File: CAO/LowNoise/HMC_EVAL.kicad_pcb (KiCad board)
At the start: 2 copper layers, 71 x 83 mm, 57 parts, among them J1 Conn_01x03, J2 Conn_01x03, Q1 IRF7319IPBF, SW1 SW_Push, U1 OPA2209, U2 HMC1001, U4 INA128

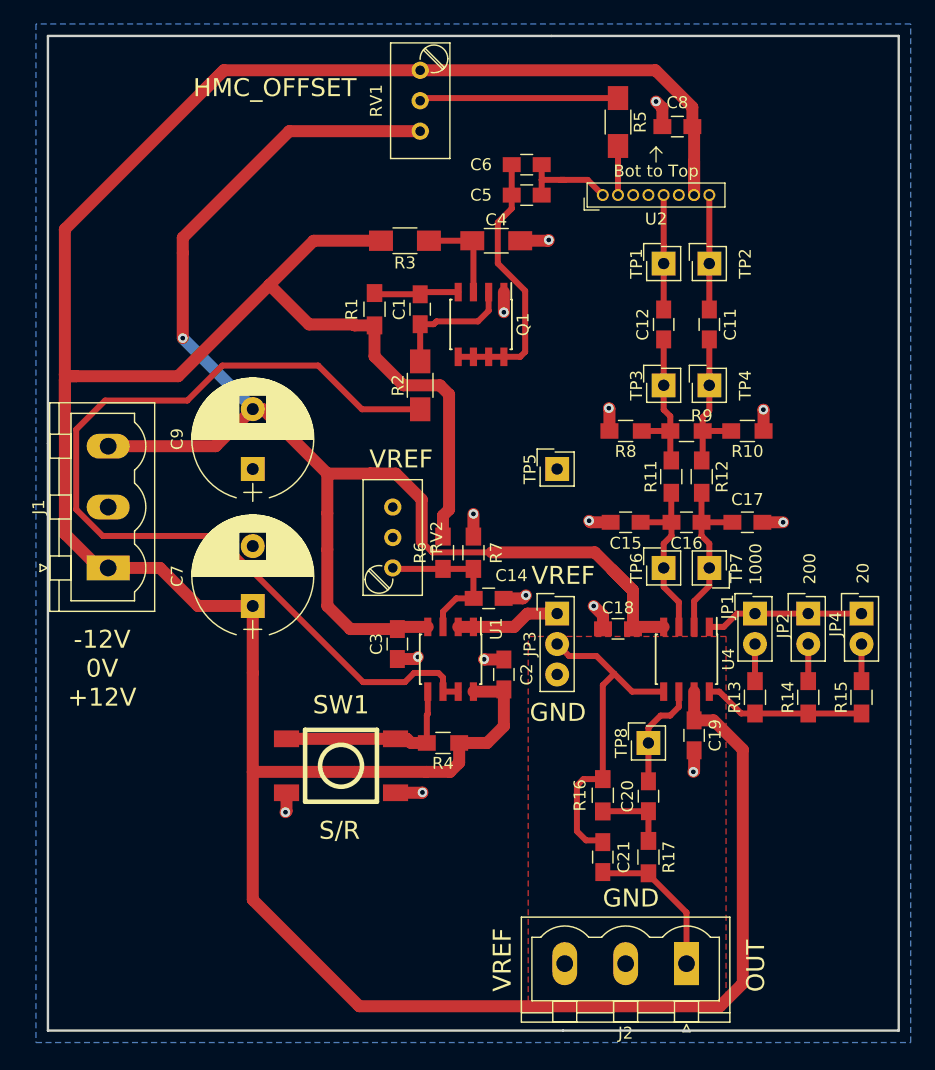
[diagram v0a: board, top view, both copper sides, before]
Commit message: - Low noise version is finish. - Add serigraphi on two design. - Qestion: Copper plane will block low freqency(200hz) magnetic wave??
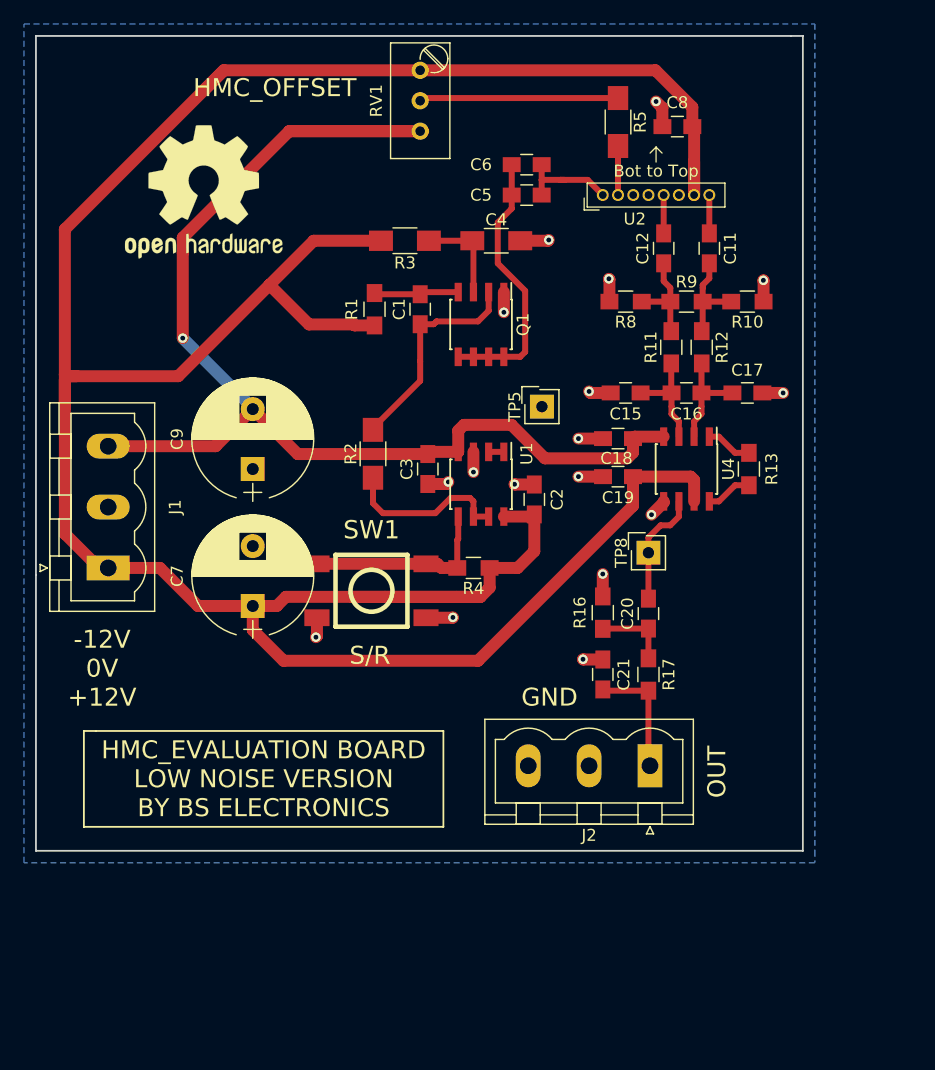
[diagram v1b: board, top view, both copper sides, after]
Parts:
- removed C14: 100nF, Capacitors_SMD:C_0805_HandSoldering
- removed JP1, JP2, JP4: Jumper, Connectors_Samtec:SL-102-X-XX_1x02
- removed JP3: Jumper_NC_Dual, Connectors_Samtec:SL-103-X-XX_1x03
- removed R14: 249, Resistors_SMD:R_0805_HandSoldering
- removed R15: 2.61k, Resistors_SMD:R_0805_HandSoldering
- removed R6, R7: R, Resistors_SMD:R_0805_HandSoldering
- removed RV2: R_POT, Potentiometers:Potentiometer_Trimmer_Bourns_3296W
- removed TP1, TP2, TP3, TP4, TP6, TP7: TestPoint, Connectors_Samtec:SL-101-X-XX_1x01
- added REF***: OSHW-Logo2_14.6x12mm_SilkScreen, Symbols:OSHW-Logo2_14.6x12mm_SilkScreen, F.Cu at (95.0, 39.7)
- moved C19 22.5 mm to (129.5, 63.5), turned to 180 degrees
- moved R13 19.1 mm to (140.5, 62.9)
- moved J2 16.8 mm to (132.2, 87.6)
- moved C18 15.9 mm to (129.5, 60.3)
- moved TP8 15.9 mm to (132.1, 69.8)
- moved U4 15.9 mm to (135.3, 62.9)
- moved R16 15.2 mm to (128.3, 74.8)
- moved C20 15.2 mm to (132.1, 74.9)
- moved C21 15.2 mm to (128.3, 80.0)
- moved R17 15.2 mm to (132.1, 80.0)
- moved C2 14.8 mm to (122.6, 65.4)
- moved C3 14.8 mm to (113.7, 62.9)
- moved U1 14.8 mm to (118.1, 64.1)
- moved R4 14.8 mm to (117.5, 71.1)
- moved SW1 14.8 mm to (109.0, 73.0)
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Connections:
- C21 pad 1: Net-(C21-Pad1) -> GNDA
- J2 pad 3: Net-(C21-Pad1) -> GNDA
- R13 pad 2: Net-(JP1-Pad2) -> Net-(R13-Pad2)
- R16 pad 1: Net-(C21-Pad1) -> GNDA
- U1 pad 3: Net-(C14-Pad2) -> GNDA
- U4 pad 1: Net-(JP1-Pad1) -> Net-(R13-Pad2)
- U4 pad 5: Net-(C21-Pad1) -> GNDA
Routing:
- net Net-(R2-Pad1): track 78.6 -> 14.0 mm
- net +12V: track 309.2 -> 253.3 mm
- net Net-(C21-Pad1): track 28.5 -> 0.00 mm
- net -12V: track 126.7 -> 105.2 mm
- net Net-(C14-Pad2): track 13.5 -> 0.00 mm
- net Net-(JP1-Pad1): track 13.2 -> 0.00 mm
- net Net-(R13-Pad1): track 13.5 -> 3.86 mm
- net Net-(U1-Pad1): track 8.71 -> 1.27 mm
- net Net-(C1-Pad1): track 10.8 -> 18.2 mm
- net Net-(C12-Pad2): track 9.55 -> 3.20 mm
- net Net-(C11-Pad1): track 9.55 -> 3.20 mm
- net Net-(C15-Pad1): track 14.6 -> 8.95 mm
- net Net-(C16-Pad1): track 14.6 -> 8.95 mm
- net Net-(C12-Pad1): track 12.7 -> 8.30 mm
- net Net-(C11-Pad2): track 12.7 -> 8.30 mm
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- removed copper zone on F.Cu, net Net-(C21-Pad1)
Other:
- board size 71 x 83 mm -> 64 x 68 mm
- board text added: "HMC_EVALUATION BOARD LOW NOISE VERSION BY BS ELECTRONICS"
- board text removed: "1000"
- board text removed: "20"
- board text removed: "200"
- board text removed: "VREF"
